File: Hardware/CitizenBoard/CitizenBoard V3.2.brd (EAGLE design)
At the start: 50 x 50 mm, 28 parts, among them IC1 MEGA8-P, J1 DCJ0202

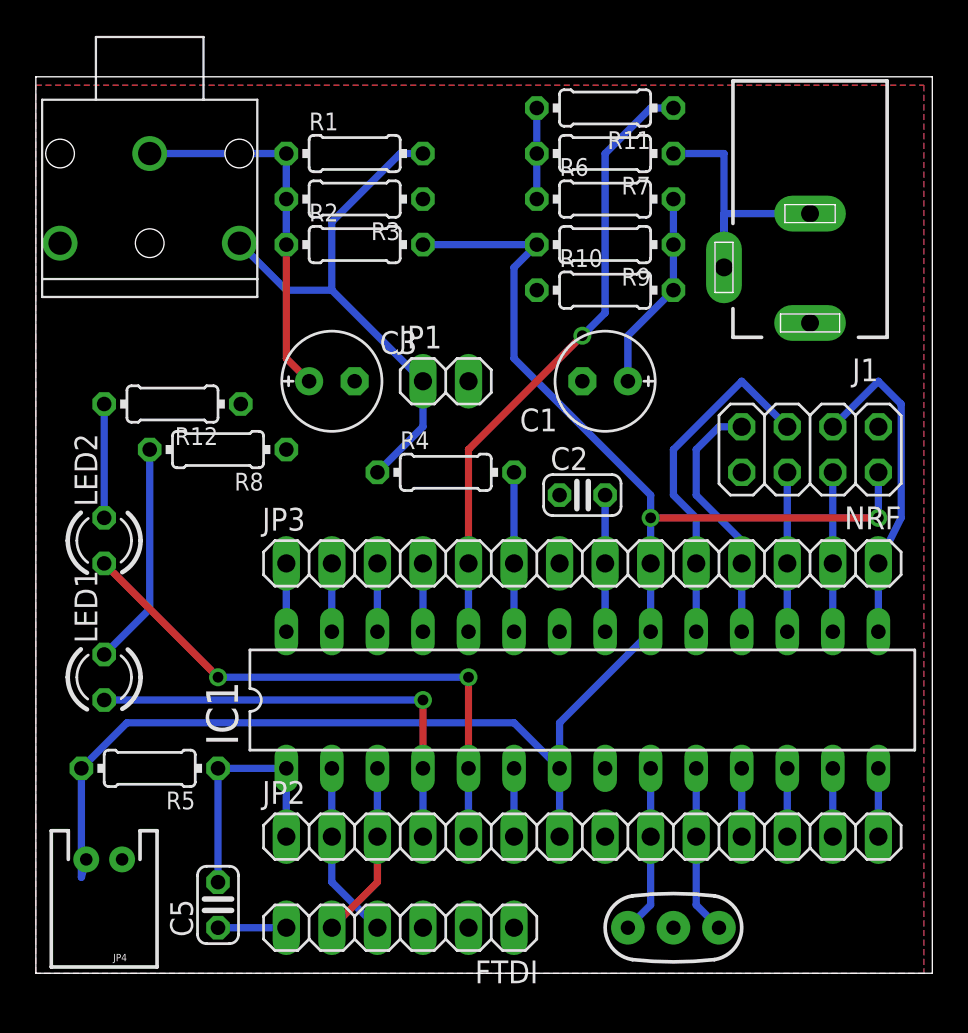
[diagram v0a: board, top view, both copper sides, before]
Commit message: Board silk fix
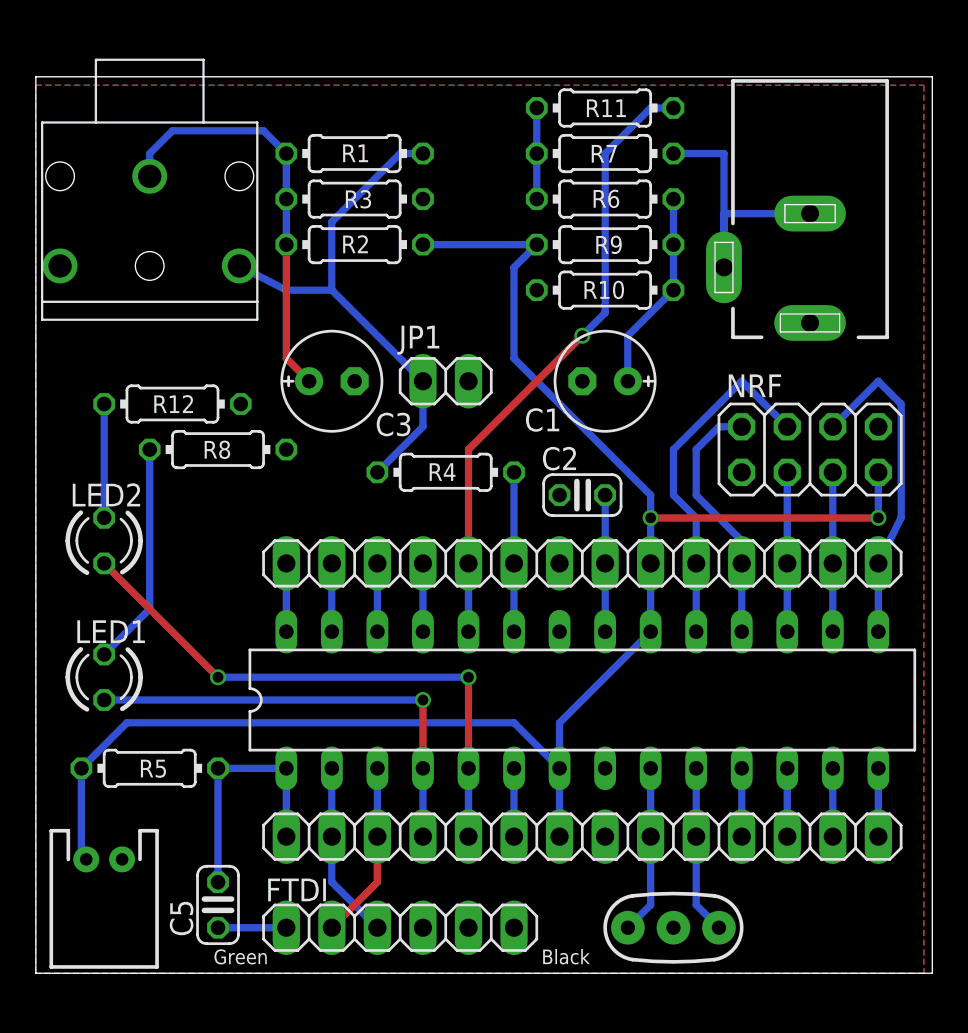
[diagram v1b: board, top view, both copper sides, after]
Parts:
- removed U$1: AUDIO-JACK-3.5, alex:AUDIO-JACK-3.5
- added J2: AUDIO-JACK-3.5, alex:AUDIO-JACK-3.5
- Y1: value (none) -> 16MHz
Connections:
- net N: now also J2.5T; no longer U$1.5T
- net N$4: now also J2.1S; no longer U$1.1S
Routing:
- net N$4: track 20.8 -> 23.2 mm
- net VCC: track 96.3 -> 94.4 mm
- net N: track 30.0 -> 29.3 mm
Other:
- board text added: "Black"
- board text added: "Green"
